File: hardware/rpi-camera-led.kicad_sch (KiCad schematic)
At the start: 20 parts, among them J1 FFC 15P 1.0mm (to Raspberry P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, J2 FFC 15P 1.0mm (to camera), J3 Qwiic (JST SH 1.0mm), J4 SWD program header 2.54mm, Q1 AO3400A, Q2 Phototransistor, U1 CH32V003J4M6

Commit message: Make R6/R7 populated 10k couplers instead of DNP 0R jumpers
The CH32V003J4M6 has no spare pins to sense the Pi-side CAM_IO pins.
With 10k always fitted between PI_IOx and CAM_IOx, the CH32 can
tri-state its pin to both pass the Pi's GPIO state through to the
camera and read it, or drive the pin to override the Pi (0.33mA worst
case through the 10k). Unpopulated-U1 pass-through still works.

Co-Authored-By: Claude Fable 5 <noreply@anthropic.com>
Claude-Session: https://claude.ai/code/session_01E6VQHygrbAGSqdngQQsBdx
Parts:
- R6, R7: value 0R (DNP) -> 10k; now fitted
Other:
- note added: "R6/R7 couple the Pi's CAM_IO pins to the camera pins/U1: with U1 high-Z (or unpopulated) the Pi's state passes through and U1 can read it; when U1 drives, it overrides the Pi through the 10k."
- note removed: "Fit R6/R7 (0R) to pass the Pi's own CAM_IO pins through when U1 is not populated. I2C and the Qwiic header work regardless."
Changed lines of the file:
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@@
   (global_label "GND" (shape bidirectional) (at 87.63 184.15 270) (fields_autoplaced yes) (effects (font (size 1.27 1.27)) (justify right)))
   (text "RPi Camera LED interposer: sits between a Raspberry Pi and its camera.\nMIPI lanes, I2C, GND and 3V3 pass straight through J1 -> J2.\nU1 (I2C slave on the camera bus) drives the camera GPIO pins 11/12,\nPWM-drives the illumination LEDs and reads ambient light on its ADC." (exclude_from_sim no) (at 20 30 0) (effects (font (size 2.0 2.0)) (justify left bottom)))
-  (text "Fit R6/R7 (0R) to pass the Pi's own CAM_IO pins through\nwhen U1 is not populated. I2C and the Qwiic header work regardless." (exclude_from_sim no) (at 108 164 0) (effects (font (size 1.27 1.27)) (justify left bottom)))
+  (text "R6/R7 couple the Pi's CAM_IO pins to the camera pins/U1: with U1\nhigh-Z (or unpopulated) the Pi's state passes through and U1 can read\nit; when U1 drives, it overrides the Pi through the 10k." (exclude_from_sim no) (at 108 164 0) (effects (font (size 1.27 1.27)) (justify left bottom)))
   (text "Pin 8 = PD1/SWIO (bonded with PD4/PD5): programming and LED gate share\nit; LEDs flicker while flashing firmware. PD1/T1CH3N gives hardware PWM." (exclude_from_sim no) (at 95 193 0) (effects (font (size 1.27 1.27)) (justify left bottom)))
   (text "LED current is set by R3/R4 against the 3V3 rail (about 30-40mA each\nwith Vf=2.9V). Total draw comes from the Pi camera 3V3 supply - keep\nthe duty/current within the Pi's camera connector budget." (exclude_from_sim no) (at 183 32 0) (effects (font (size 1.27 1.27)) (justify left bottom)))
@@
   )
   (symbol (lib_id "Device:R") (at 152.4 129.54 0) (unit 1)
-    (exclude_from_sim no) (in_bom yes) (on_board yes) (dnp yes)
+    (exclude_from_sim no) (in_bom yes) (on_board yes) (dnp no)
     (property "Reference" "R6" (at 154.4 123.54 0) (effects (font (size 1.27 1.27)) ))
-    (property "Value" "0R (DNP)" (at 154.4 135.54 0) (effects (font (size 1.27 1.27)) ))
+    (property "Value" "10k" (at 154.4 135.54 0) (effects (font (size 1.27 1.27)) ))
     (property "Footprint" "Resistor_SMD:R_0402_1005Metric" (at 152.4 129.54 0) (effects (font (size 1.27 1.27)) (hide yes)))
     (property "Datasheet" "" (at 152.4 129.54 0) (effects (font (size 1.27 1.27)) (hide yes)))
@@
   )
   (symbol (lib_id "Device:R") (at 163.83 129.54 0) (unit 1)
-    (exclude_from_sim no) (in_bom yes) (on_board yes) (dnp yes)
+    (exclude_from_sim no) (in_bom yes) (on_board yes) (dnp no)
     (property "Reference" "R7" (at 165.83 123.54 0) (effects (font (size 1.27 1.27)) ))
-    (property "Value" "0R (DNP)" (at 165.83 135.54 0) (effects (font (size 1.27 1.27)) ))
+    (property "Value" "10k" (at 165.83 135.54 0) (effects (font (size 1.27 1.27)) ))
     (property "Footprint" "Resistor_SMD:R_0402_1005Metric" (at 163.83 129.54 0) (effects (font (size 1.27 1.27)) (hide yes)))
     (property "Datasheet" "" (at 163.83 129.54 0) (effects (font (size 1.27 1.27)) (hide yes)))

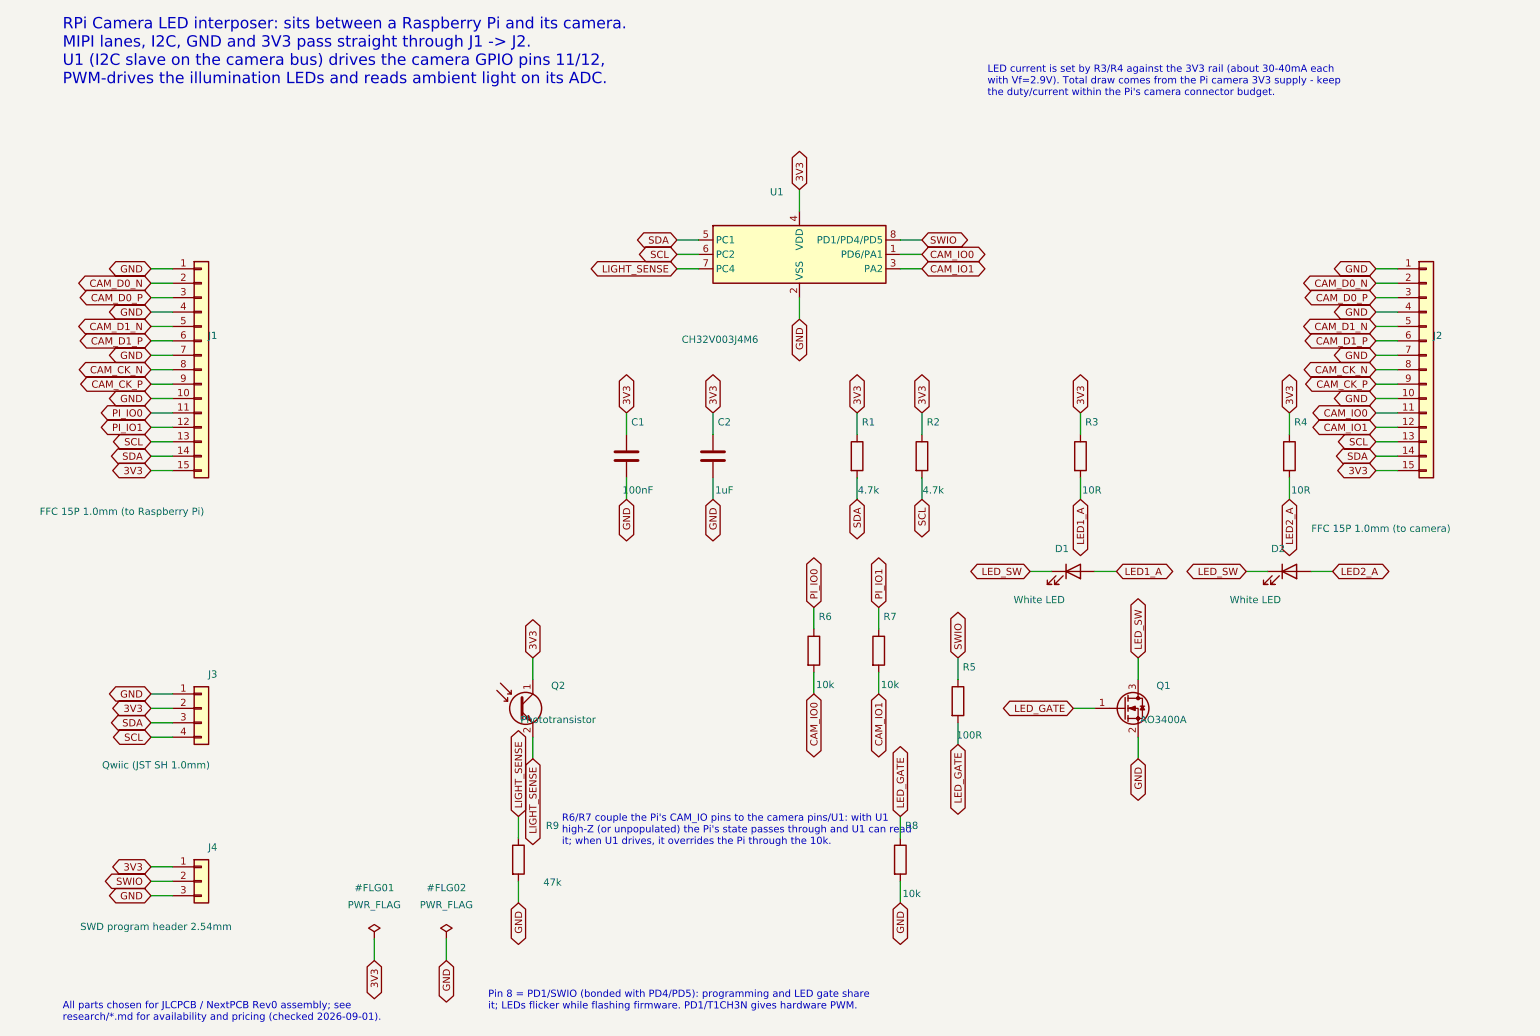
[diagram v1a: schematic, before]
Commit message: Wire the schematic connections directly in eeschema
Hand edits made in the schematic editor: most of the generated
global-label stubs are replaced by real wires and junctions between
adjacent parts (78 -> 86 wires, 0 -> 8 junctions), so connectivity is
visible on the sheet rather than implied by matching label names.  GND
picks up a power symbol and the remaining single labels now just name
their nets: GND 17 -> 9 labels, LED1_A/LED2_A 2 -> 1, LED_GATE 3 -> 1,
LIGHT_SENSE 3 -> 2.

U1's value becomes CH32V003A4M6; its symbol and footprint still have to
follow it to SOP-16, which is the next commit.

Verified no connections moved: kicad-cli ERC reports only the known
MCU_WCH_RiscV-not-in-global-table warning, and the exported netlist
still matches every net in hardware/tools/check_schematic.py.

The .kicad_pro hunk is just the default ERC severity/pin-map block that
eeschema writes out the first time it saves a project.

Co-Authored-By: Claude Opus 5 (1M context) <noreply@anthropic.com>
Claude-Session: https://claude.ai/code/session_01E6VQHygrbAGSqdngQQsBdx
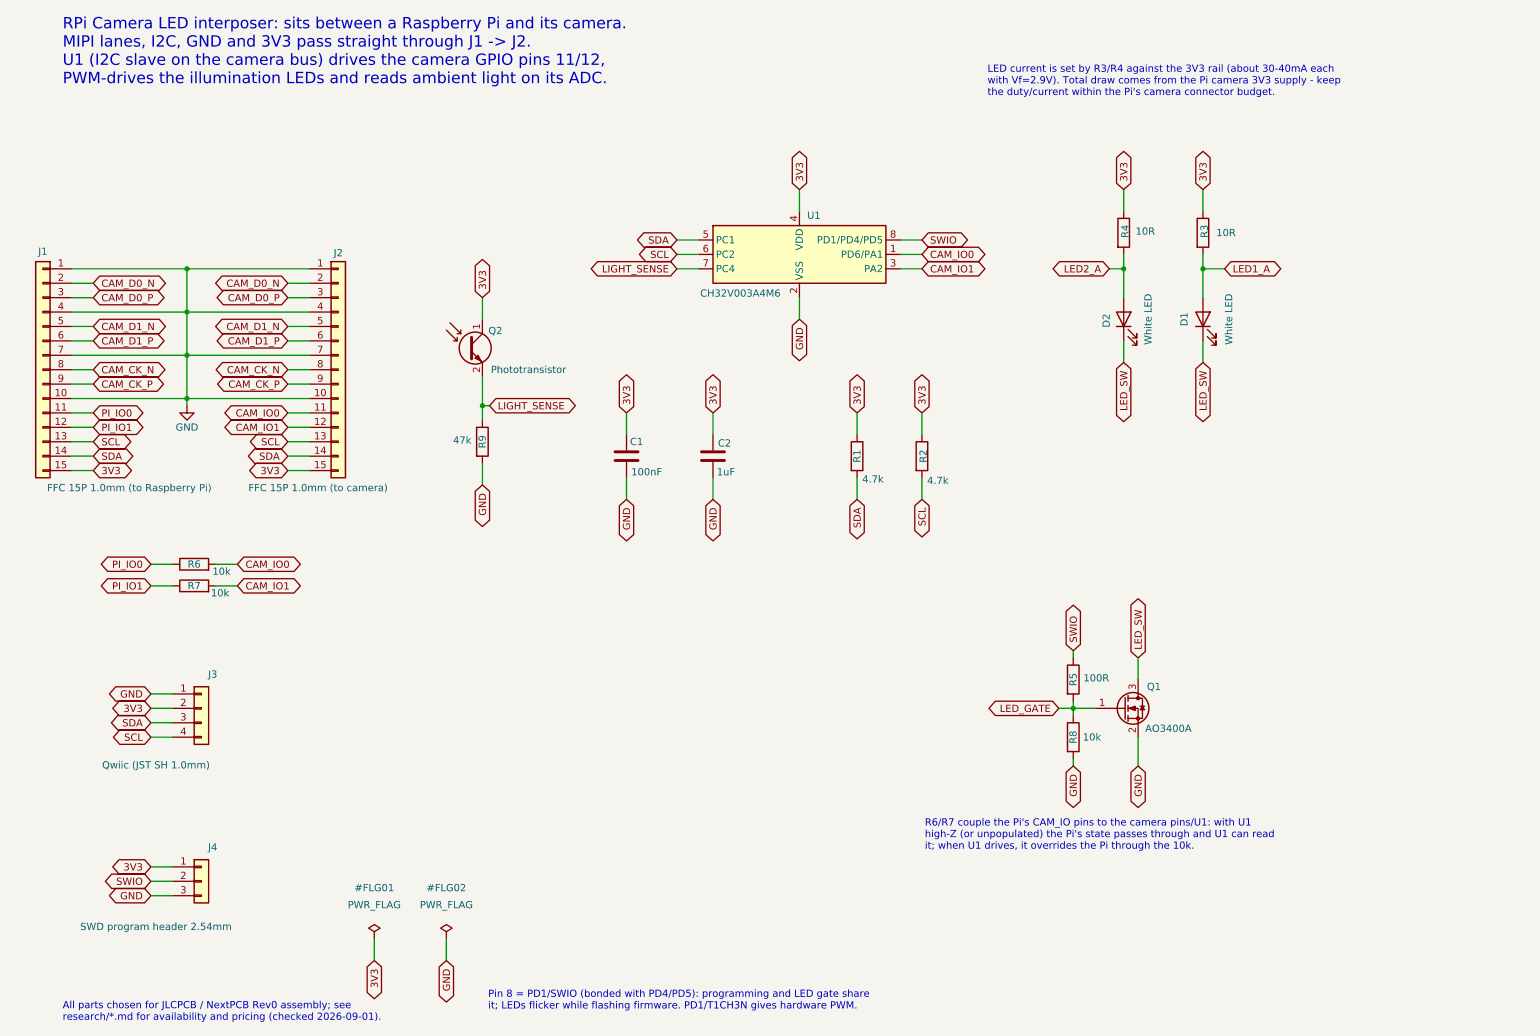
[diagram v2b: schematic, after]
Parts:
- U1: value CH32V003J4M6 -> CH32V003A4M6
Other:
- moved on the sheet: D1, D2, J1, J2, Q2, R3, R4, R5, R6, R7, R8, R9

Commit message: Move U1 to the CH32V003A4M6 in SOP-16
Swap the SOP-8 CH32V003JxMx symbol for KiCad's CH32V003AxMx and the
SOIC-8 footprint for SOIC-16_3.9x9.9mm_P1.27mm, matching the value Tim
set.  Pin assignment, against WCH's CH32V003 datasheet V1.8 table 2-1
(which tabulates SOP16 alongside the other packages):

    1  PC1  SDA           10  PD6  CAM_IO0
    2  PC2  SCL           13  PA2  CAM_IO1
    3  PC3  LED_PWM       14  VSS  GND
    4  PC4  LIGHT_SENSE   15  VDD  3V3
    7  PD1  SWIO

PC1/PC2/PC4/PD6/PA2 keep the ports they had on SOP-8, so the I2C
peripheral, the ADC channel (A2) and the GPIO pass-through code carry
over unchanged.

The package earns its extra 8 pins by undoing the SOP-8 compromises.
No pin bonds two ports any more, so the floating-input dance that kept
PA1/PD4/PD5 off the shared pins is no longer needed.  More importantly
the LED gate moves off the debug pin: PC3 is TIM1 CH3, a true output
rather than the complementary CH3N, so R5 is now fed from its own pin
(new LED_PWM net) and the LEDs no longer flicker while flashing.  PD1
carries SWIO alone.

PC6, PC7, PD4, PD5, PD7/NRST, PA1 and PC0 are spare and carry explicit
no-connects, so ERC still passes with pin_not_connected as an error.

check_schematic.py follows the pin moves and gains a coverage check
that every U1 pin is either in a net or listed as deliberately unused,
so a pin cannot be silently dropped by a future repackage.  ERC is
clean bar the known MCU_WCH_RiscV library warning and the netlist
matches design intent.

Part is stocked by both assemblers: JLCPCB C5346357 at $0.2152/100
(1,907 in stock), HQ Online/NextPCB Rev0 at $0.2008/100 -- about 3
cents more than the SOP-8.

Co-Authored-By: Claude Opus 5 (1M context) <noreply@anthropic.com>
Claude-Session: https://claude.ai/code/session_01E6VQHygrbAGSqdngQQsBdx
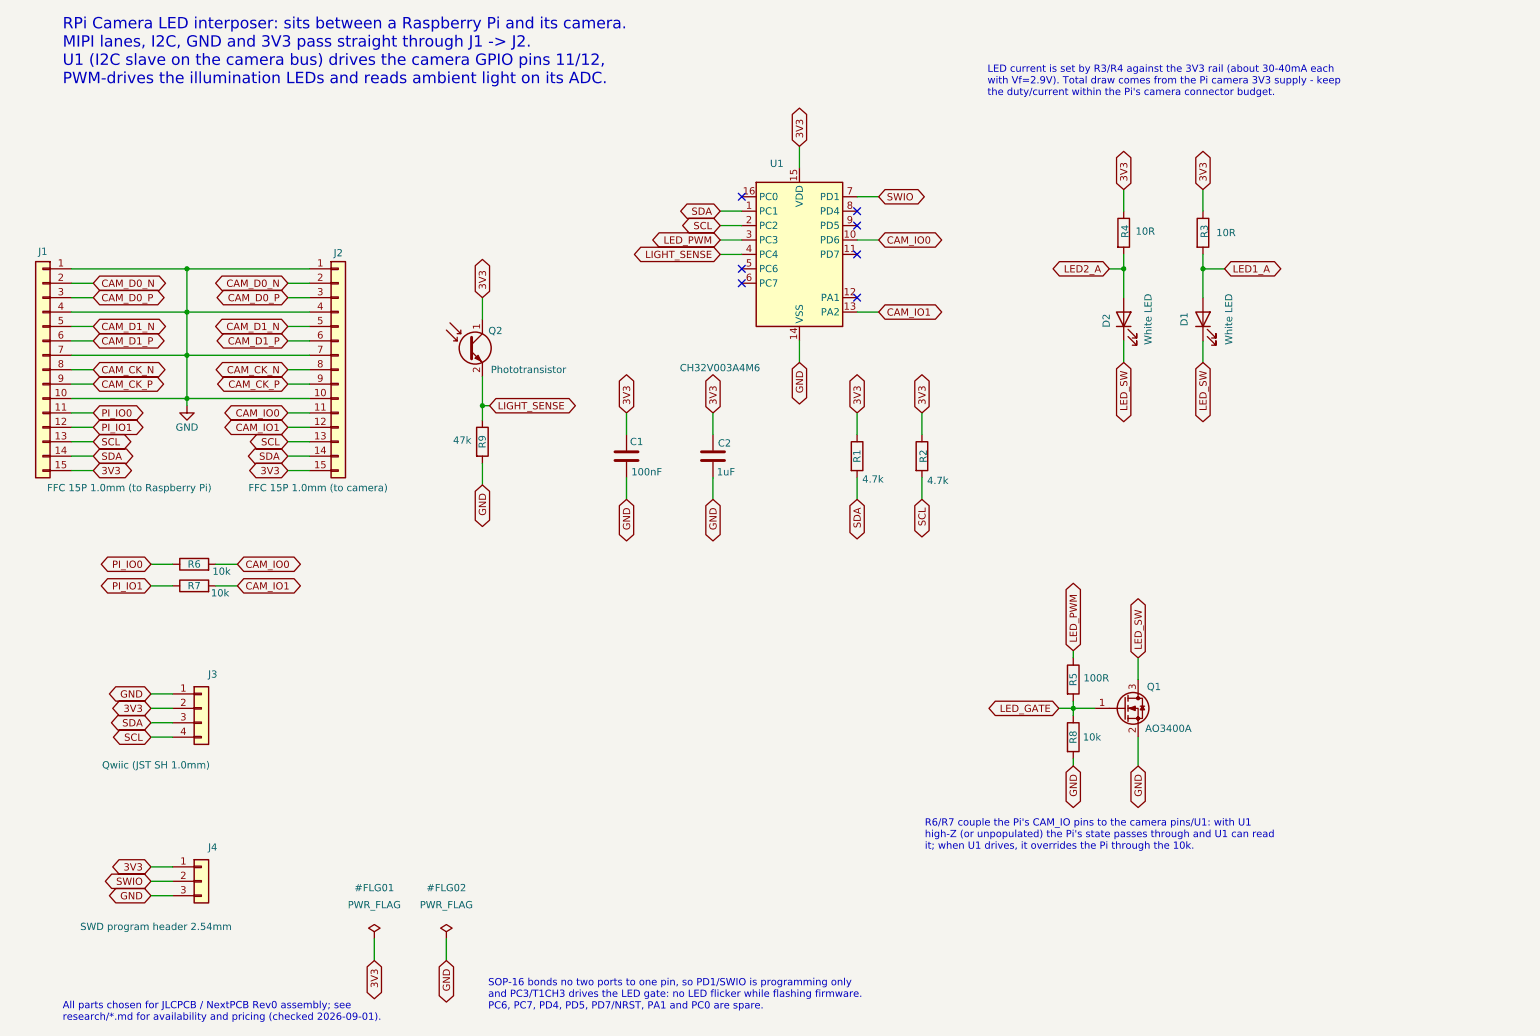
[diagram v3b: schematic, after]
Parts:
- removed U1: CH32V003A4M6, Package_SO:SOIC-8_3.9x4.9mm_P1.27mm, symbol MCU_WCH_RiscV:CH32V003JxMx
- added U1: CH32V003A4M6, Package_SO:SOIC-16_3.9x9.9mm_P1.27mm, symbol MCU_WCH_RiscV:CH32V003AxMx
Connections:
- net 3V3: now also U1.15 (VDD)
- net CAM_IO0: now also U1.10 (PD6)
- net CAM_IO1: now also U1.13 (PA2)
- net GND: now also U1.14 (VSS)
- net LIGHT_SENSE: now also U1.4 (PC4)
- net SCL: now also U1.2 (PC2)
- net SDA: now also U1.1 (PC1)
- net SWIO: now also U1.7 (PD1); no longer R5.1
- new net LED_PWM: R5.1, U1.3 (PC3)
- no-connect marks 0 -> 7
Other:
- note added: "SOP-16 bonds no two ports to one pin, so PD1/SWIO is programming only and PC3/T1CH3 drives the LED gate: no LED flicker while flashing firmware. PC6, PC7, PD4, PD5, PD7/NRST, PA1 and PC0 are spare."
- note removed: "Pin 8 = PD1/SWIO (bonded with PD4/PD5): programming and LED gate share it; LEDs flicker while flashing firmware. PD1/T1CH3N gives hardware PWM."

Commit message: Give U1 dedicated Pi-sense and camera-drive pins
Rework the camera GPIO section now that SOP-16 has pins to spare, and
redraw J1/J2 as facing connector blocks so the pass-through nets read
straight across the sheet.

U1 no longer shares one pin per channel with the coupler.  It sits
across it instead: PD6/PD7 (pins 10/11) watch the Pi side and PA1/PA2
(pins 12/13) drive the camera side, so reading the Pi no longer means
tri-stating the pin that drives the camera.  R6/R7 drop from 10k to 0R,
turning them from couplers into a straight bypass link.

Two things this leaves open, both flagged rather than guessed at:

  * PD7 (pin 11) carries the PI_IO0 label, the same net as PD6 (pin
    10), while PI_IO1 has no U1 pin at all.  The symmetry of the other
    three pins suggests pin 11 was meant to be PI_IO1.
  * PD7 is the NRST pin until the RST_MODE option byte in flash says
    otherwise, so it cannot be used as a plain input out of the box.

check_schematic.py is therefore red on PI_IO0/CAM_IO0 by design: its
expected nets still describe the coupler wiring, and updating them now
would bless the pin 11 label before it is settled.

Co-Authored-By: Claude Opus 5 (1M context) <noreply@anthropic.com>
Claude-Session: https://claude.ai/code/session_01E6VQHygrbAGSqdngQQsBdx
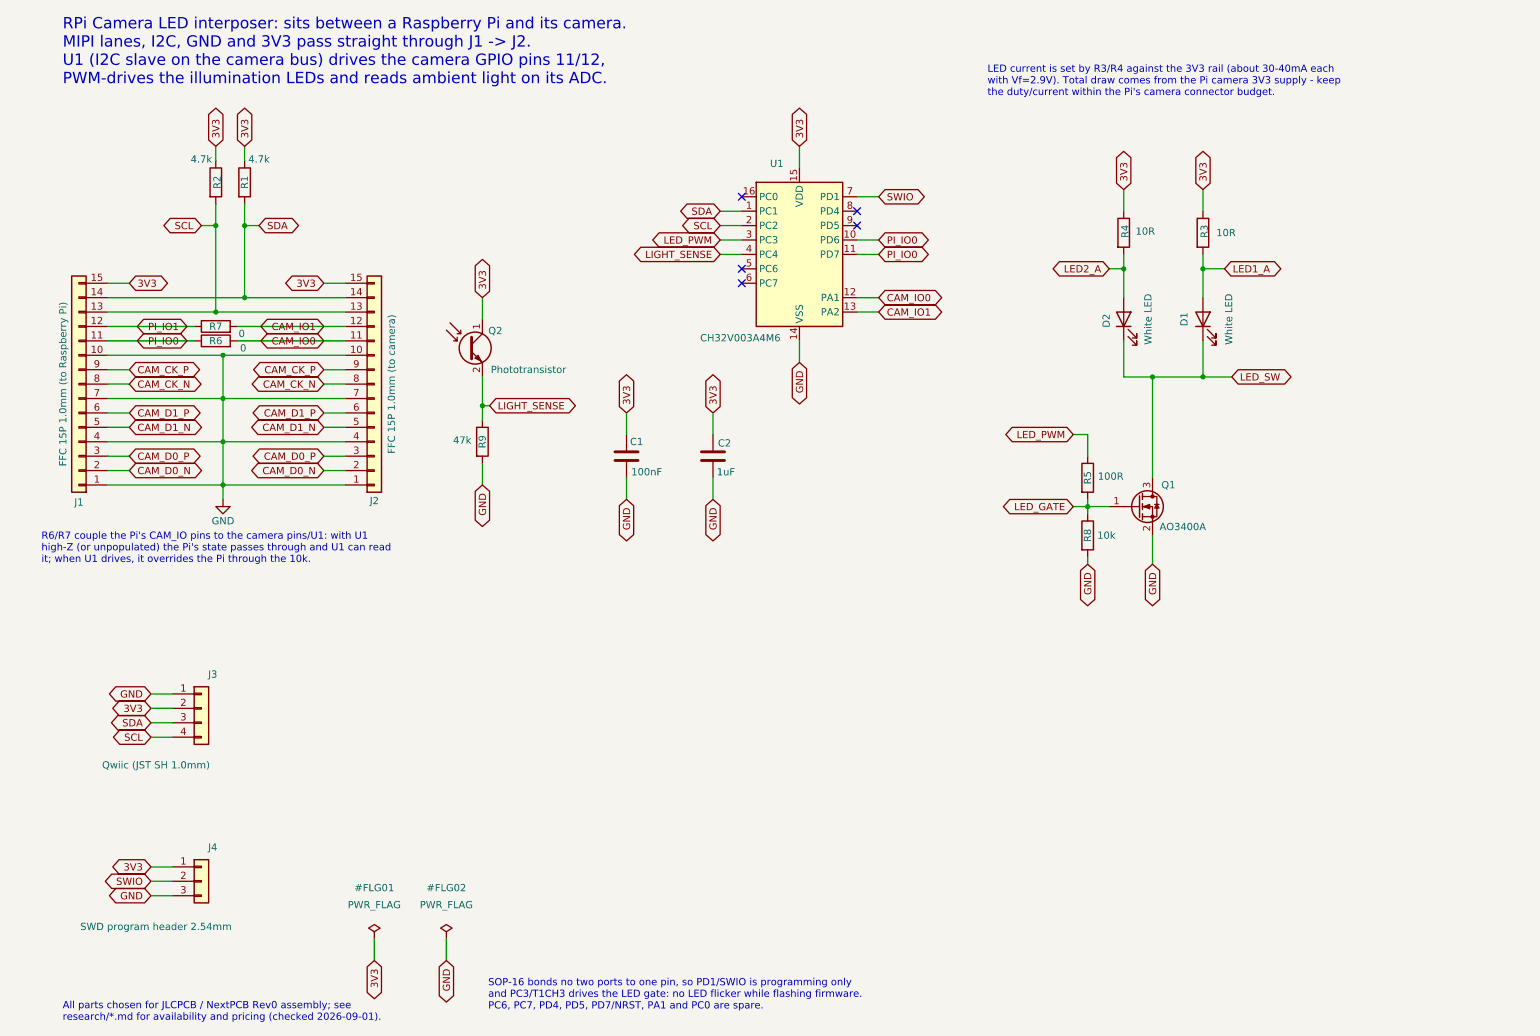
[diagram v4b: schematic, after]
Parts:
- R6, R7: value 10k -> 0
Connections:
- net CAM_IO0: now also U1.12 (PA1); no longer U1.10 (PD6)
- net PI_IO0: now also U1.10 (PD6), U1.11 (PD7)
- no-connect marks 7 -> 5
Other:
- moved on the sheet: J1, J2, Q1, R1, R2, R5, R6, R7, R8
